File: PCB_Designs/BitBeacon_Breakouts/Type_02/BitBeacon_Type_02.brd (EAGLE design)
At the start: 30.5 x 33 mm, 100 parts, among them IC1 AD8603UJ, IC2 AD8603UJ, IC3 AD8603UJ, IC4 AD8603UJ

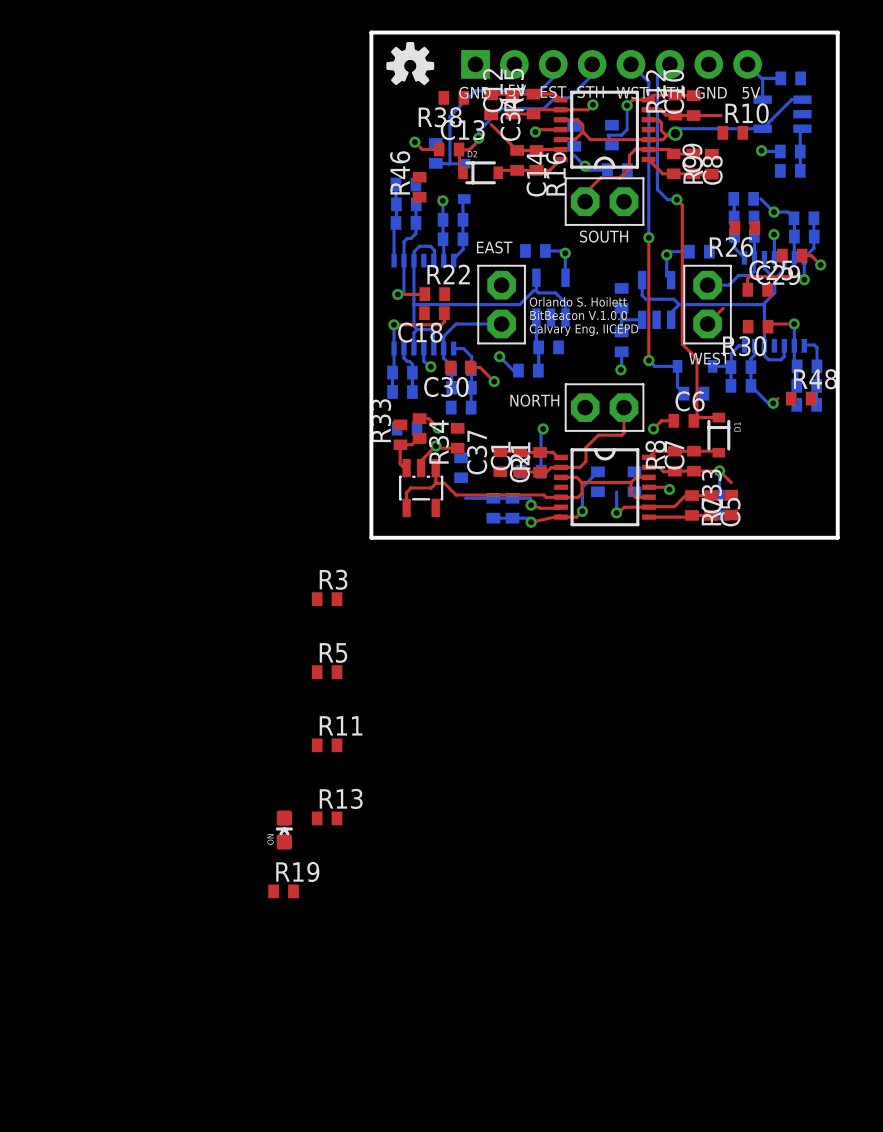
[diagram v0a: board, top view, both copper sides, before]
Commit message: updates to code to include Bluetooth, updates to BitBeacon circuit to include labels, indicator LEDs, added BitBeacon Breakout to prototype different signal amplifier types
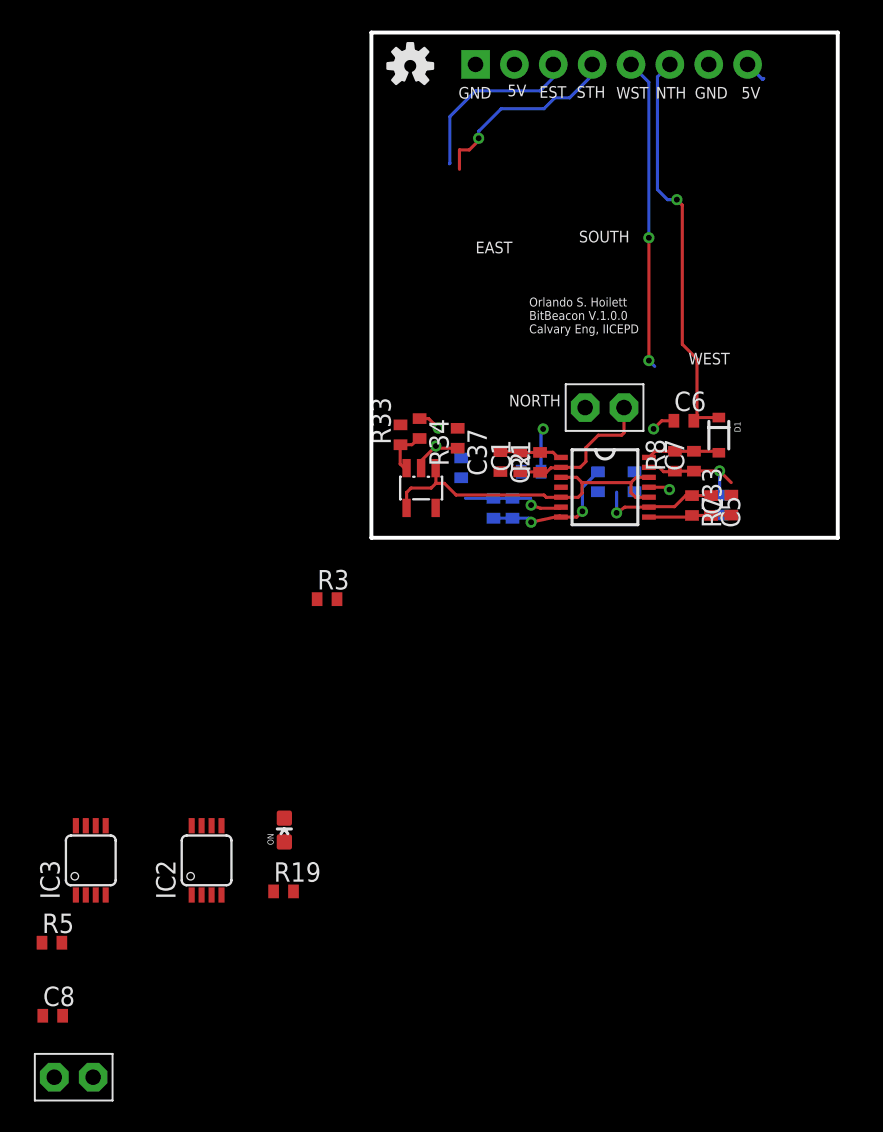
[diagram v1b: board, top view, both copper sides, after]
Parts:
- removed C10, C12, C14, C15, C17, C19, C21, C22, C24, C26, C28: 22p, resistor:C0402
- removed C11, C16, C18, C23, C25, C34, C35, C36, C9: (no value), resistor:C0402
- removed C13, C20, C27, C29, C30, C31, C38, C39, C40: 100n, resistor:C0402
- removed D2, D3, D4: 250mA/100V, SparkFun-DiscreteSemi:SOD-323
- removed E-AMP, S-AMP, W-AMP: AD8609RU, analog-devices:TSSOP14
- removed E-PD1, S-PD1, W-PD1: BPW46, Orlando:PIN-PHOTODIODE
- removed IC4: AD8603UJ, analog-devices:SOT23-5
- removed R10, R14, R18, R22, R26, R30, R38, R39, R40, R41, R42, R43, R44, R46, R48: (no value), resistor:R0402
- removed R11, R12, R13, R15, R16, R20, R23, R24, R28, R31, R32: 1M, resistor:R0402
- removed R17, R25, R9: 1k, resistor:R0402
- added N-PD2: BPW46, Orlando:PIN-PHOTODIODE
- C8: value 22p -> 700p
- IC2, IC3: value AD8603UJ -> AD8607RM; device analog-devices:SOT23-5 -> analog-devices:MSOP08
- R5: value 1M -> 22k
- moved C8 69.7 mm to (-20.8, -31.2), turned to 0 degrees
- moved IC2 61.6 mm to (-10.8, -21.1), flipped to the top, turned to 0 degrees
- moved IC3 47.5 mm to (-18.3, -21.1), flipped to the top
- moved R5 25.2 mm to (-20.9, -26.5)
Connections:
- removed net 1/2-VDD-E: E-AMP.10, E-AMP.12, E-AMP.3, E-AMP.5, IC3.1, IC3.4
- removed net 1/2-VDD-S: IC2.1, IC2.4, S-AMP.10, S-AMP.12, S-AMP.3, S-AMP.5
- removed net 1/2-VDD-W: IC4.1, IC4.4, W-AMP.10, W-AMP.12, W-AMP.3, W-AMP.5
- removed net N$12: C10.1, R10.1, R12.1, S-AMP.6
- removed net N$13: C10.2, C11.1, R12.2, S-AMP.7
- removed net N$14: C12.1, R14.1, R15.1, S-AMP.9
- removed net N$15: C12.2, C34.1, R15.2, S-AMP.8
- removed net N$16: IC2.3, R39.1, R40.2
- removed net N$17: IC3.3, R41.1, R42.2
- removed net N$18: IC4.3, R43.1, R44.2
- removed net N$19: C15.1, E-AMP.2, E-PD1.2, R17.1
- removed net N$20: C15.2, C16.1, E-AMP.1, R17.2
- removed net N$21: C17.1, E-AMP.6, R18.1, R20.1
- removed net N$22: C17.2, C18.1, E-AMP.7, R20.2
- removed net N$23: C19.1, E-AMP.9, R22.1, R23.1
- removed net N$24: C19.2, C35.1, E-AMP.8, R23.2
- removed net N$25: C28.1, R32.1, R48.1, W-AMP.13
- removed net N$26: C21.1, E-AMP.13, R24.1, R46.1
- removed net N$28: C22.1, R25.1, W-AMP.2, W-PD1.2
- removed net N$29: C22.2, C23.1, R25.2, W-AMP.1
- removed net N$30: C24.1, R26.1, R28.1, W-AMP.6
- removed net N$31: C24.2, C25.1, R28.2, W-AMP.7
- removed net N$32: C26.1, R30.1, R31.1, W-AMP.9
- removed net N$33: C26.2, C36.1, R31.2, W-AMP.8
- removed net N$36: C34.2, R38.2
- removed net N$37: C11.2, R14.2
- removed net N$38: C9.2, R10.2
- removed net N$39: C35.2, R46.2
- removed net N$40: C18.2, R22.2
- removed net N$41: C16.2, R18.2
- removed net N$42: C36.2, R48.2
- removed net N$43: C25.2, R30.2
- removed net N$44: C14.2, D2.A, R16.2, S-AMP.14
- removed net N$45: C23.2, R26.2
- removed net N$46: C21.2, D3.A, E-AMP.14, R24.2
- removed net N$47: C28.2, D4.A, R32.2, W-AMP.14
- removed net S-AMP: C8.2, C9.1, R9.2, S-AMP.1
- new net V+: IC2.8, IC3.8
- new net V-: IC2.4, IC3.4
- new net VREF: IC2.3
- net 5V: no longer C29.2, C30.2, C31.2, C38.1, C39.1, C40.1, E-AMP.4, IC2.5, IC3.5, IC4.5, R39.2, R41.2, R43.2, S-AMP.4, W-AMP.4
- net E-OUT: no longer C20.2, D3.C, R11.2
- net GND: now also N-PD2.1; no longer C13.1, C20.1, C27.1, C29.1, C30.1, C31.1, C38.2, C39.2, C40.2, E-AMP.11, E-PD1.1, IC2.2, IC3.2, IC4.2, R11.1, R13.1, R40.1, R42.1, R44.1, R5.1, S-AMP.11, S-PD1.1, W-AMP.11, W-PD1.1
- net N$2: now also C8.1, IC2.2, N-PD2.2, R5.1; no longer C14.1, R16.1, R38.1, S-AMP.13
- net N$4: now also C8.2, IC2.1, R5.2; no longer C8.1, R9.1, S-AMP.2, S-PD1.2
- net S-OUT: no longer C13.2, D2.C, R5.2
- net W-OUT: no longer C27.2, D4.C, R13.2
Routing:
- net 1/2-VDD-E: track 23.5 -> 0.00 mm
- net 1/2-VDD-S: track 21.3 -> 0.00 mm, vias 1 -> 0
- net 1/2-VDD-W: track 21.3 -> 0.00 mm
- net 5V: track 22.7 -> 4.35 mm, vias 9 -> 1
- net N$4: track 9.43 -> 0.00 mm
- net N$31: track 8.88 -> 0.00 mm, vias 1 -> 0
- net N$23: track 8.51 -> 0.00 mm, vias 1 -> 0
- net N$22: track 8.39 -> 0.00 mm, vias 1 -> 0
- net GND: track 16.1 -> 7.76 mm, vias 8 -> 4
- net N$13: track 8.28 -> 0.00 mm, vias 1 -> 0
- net N$19: track 7.69 -> 0.00 mm
- net N$28: track 6.97 -> 0.00 mm
- net N$32: track 5.66 -> 0.00 mm, vias 1 -> 0
- net N$30: track 5.58 -> 0.00 mm, vias 1 -> 0
- net N$14: track 5.51 -> 0.00 mm, vias 1 -> 0
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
